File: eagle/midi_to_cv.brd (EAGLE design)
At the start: 100 x 80 mm, 75 parts, among them IC1 TL082P, IC2 TL084P, IC4 TL082P, IC6 TL082P, IC7 TL082P, U1 ATMEGA328P_PDIP, U2 MCP4822-E/P, U3 MCP4822-E/P, U4 MCP4822-E/P, U5 MCP4822-E/P

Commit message: nearly routable
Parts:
- moved R28 6.35 mm to (74.9, 43.2), turned to 270 degrees
- moved R15 5.39 mm to (12.7, 59.7), turned to 0 degrees
- moved R24 5.24 mm to (11.4, 64.8)
- moved R5 4.58 mm to (72.4, 59.7)
- moved R20 3.81 mm to (88.9, 11.4)
- moved R3 3.59 mm to (15.2, 34.3), turned to 180 degrees
- moved PAD23 2.54 mm to (21.6, 73.7)
- moved U3 2.54 mm to (20.3, 55.9)
- moved R21 2.54 mm to (83.8, 11.4)
- moved PAD6 1.80 mm to (53.3, 71.1)
- moved R29 1.80 mm to (80.0, 41.9), turned to 90 degrees
- moved IC1 1.80 mm to (53.3, 62.2)
- moved R10 1.27 mm to (41.9, 72.4)
- moved R11 1.27 mm to (58.4, 74.9)
- moved R4 1.27 mm to (50.8, 50.8)
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
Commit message: hand routing
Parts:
- moved PAD2 15.3 mm to (14.0, 15.2)
- moved PAD20 10.8 mm to (31.2, 32.3)
- moved D1 8.52 mm to (15.2, 24.1), turned to 270 degrees
- moved PAD5 5.06 mm to (90.4, 53.6)
- moved PAD12 4.58 mm to (11.4, 38.1)
- moved R3 4.02 mm to (14.0, 38.1), turned to 90 degrees
- moved R2 3.81 mm to (11.4, 25.4)
- moved R12 3.07 mm to (82.5, 53.6)
- moved PAD21 3.07 mm to (35.8, 24.1)
- moved OK1 2.84 mm to (24.1, 22.9), turned to 270 degrees
- moved PAD22 2.84 mm to (35.8, 28.7)
- moved R13 2.59 mm to (84.3, 50.8)
- moved IC2 2.54 mm to (58.4, 14.0)
- moved R1 2.54 mm to (7.62, 25.4), turned to 90 degrees
- moved PAD14 1.80 mm to (20.3, 11.4)
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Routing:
- net GND: track 0.00 -> 267.4 mm
- net +12V: track 0.00 -> 263.1 mm
- net +5V: track 0.00 -> 124.4 mm
- net -12V: track 0.00 -> 120.8 mm
- net N$41: track 0.00 -> 33.8 mm
- net N$30: track 0.00 -> 31.7 mm
- net N$59: track 0.00 -> 24.6 mm
- net N$1: track 0.00 -> 23.0 mm
- net N$22: track 0.00 -> 20.9 mm
- net N$36: track 0.00 -> 20.7 mm
- net N$35: track 0.00 -> 18.3 mm
- net N$50: track 0.00 -> 18.3 mm
- net N$18: track 0.00 -> 17.9 mm
- net N$39: track 0.00 -> 17.6 mm
- net N$27: track 0.00 -> 17.1 mm
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
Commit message: manually routed and vias adjusted
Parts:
- moved PAD18 4.57 mm to (49.5, 13.5)
- moved PAD16 4.07 mm to (67.1, 16.3)
- moved PAD11 3.66 mm to (55.1, 51.3)
- moved R4 2.59 mm to (48.3, 51.3)
- moved PAD8 2.29 mm to (67.3, 21.8)
- moved R16 2.05 mm to (71.6, 11.2), turned to 270 degrees
- moved PAD7 1.61 mm to (67.8, 6.10)
- moved PAD10 1.27 mm to (49.5, 6.35)
- moved R3 1.05 mm to (14.2, 39.1)
- moved R28 0.92 mm to (74.4, 42.4)
- moved PAD4 0.51 mm to (47.0, 74.4)
- moved R18 0.51 mm to (36.8, 10.7)
- moved R19 0.51 mm to (44.5, 10.7)
- moved R22 0.51 mm to (33.0, 10.7)
- moved R23 0.51 mm to (40.6, 10.7)
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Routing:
- net -12V: track 120.8 -> 233.8 mm, vias 0 -> 6
- net +5V: track 124.4 -> 218.0 mm, vias 0 -> 4
- net GND: track 267.4 -> 324.0 mm
- net N$42: track 5.08 -> 30.2 mm
- net N$24: track 0.00 -> 24.8 mm, vias 0 -> 2
- net N$37: track 0.00 -> 20.9 mm
- net N$39: track 17.6 -> 38.2 mm
- net +12V: track 263.1 -> 278.8 mm, vias 0 -> 2
- net N$61: track 0.00 -> 11.8 mm
- net N$40: track 11.7 -> 23.0 mm
- net N$38: track 0.00 -> 10.2 mm
- net N$35: track 18.3 -> 9.44 mm
- net N$56: track 0.00 -> 7.32 mm
- net N$34: track 0.00 -> 5.92 mm
- net N$44: track 0.00 -> 5.61 mm
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
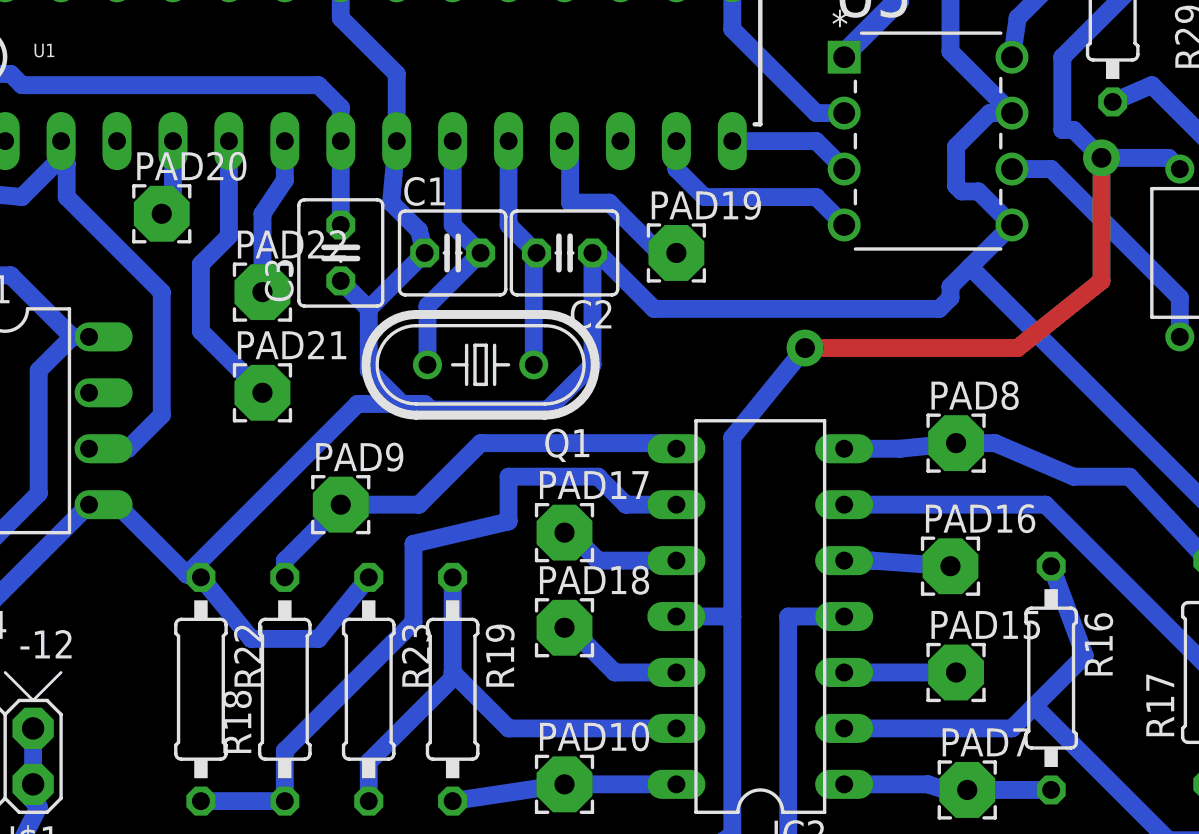
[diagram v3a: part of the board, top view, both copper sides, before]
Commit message: will route gates to op amps instead of jumper pads
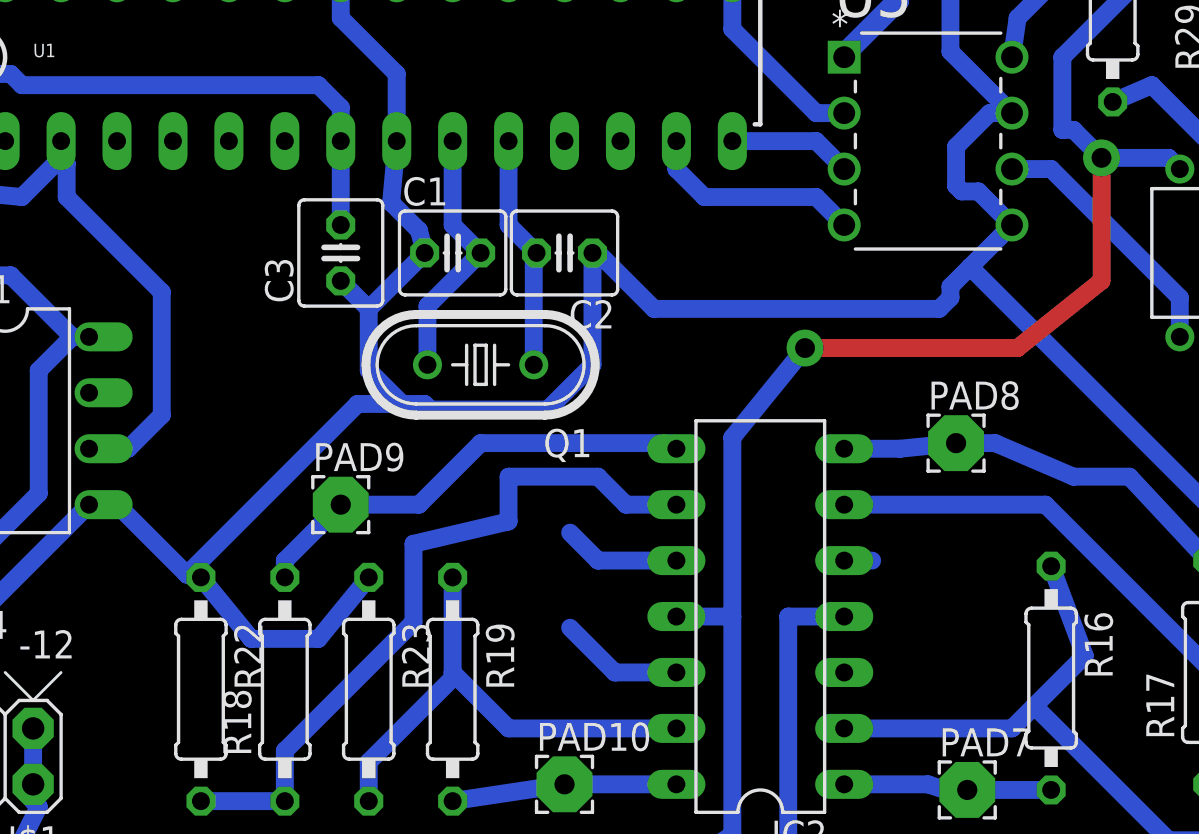
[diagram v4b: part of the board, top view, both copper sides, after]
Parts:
- removed PAD15, PAD16, PAD17, PAD18, PAD19, PAD20, PAD21, PAD22: gate, wirepad:2,54/0,9
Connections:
- removed net N$31: PAD19.1, U1.11
- removed net N$32: PAD20.1, U1.4
- removed net N$33: PAD21.1, U1.5
- removed net N$43: PAD22.1, U1.6
- net N$34: now also U1.11; no longer PAD18.1
- net N$44: now also U1.6; no longer PAD17.1
- net N$45: now also U1.5; no longer PAD16.1
- net N$46: now also U1.4; no longer PAD15.1
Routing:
- net N$33: track 13.1 -> 0.00 mm
- net N$31: track 8.67 -> 0.00 mm
- net N$43: track 7.17 -> 0.00 mm
- net N$46: track 5.08 -> 0.00 mm
- net N$45: track 4.84 -> 1.27 mm
- net N$32: track 3.51 -> 0.00 mm
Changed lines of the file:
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@@
 <element name="PAD13" library="wirepad" package="2,54/0,9" value="reset " x="69.85" y="73.66"/>
 <element name="PAD14" library="wirepad" package="2,54/0,9" value="gate LED" x="20.32" y="11.43"/>
-<element name="PAD15" library="wirepad" package="2,54/0,9" value="gate" x="67.31" y="11.43"/>
-<element name="PAD16" library="wirepad" package="2,54/0,9" value="gate" x="67.056" y="16.256"/>
-<element name="PAD17" library="wirepad" package="2,54/0,9" value="gate" x="49.53" y="17.78"/>
-<element name="PAD18" library="wirepad" package="2,54/0,9" value="gate" x="49.53" y="13.462"/>
-<element name="PAD19" library="wirepad" package="2,54/0,9" value="gate" x="54.61" y="30.48"/>
-<element name="PAD20" library="wirepad" package="2,54/0,9" value="gate" x="31.242" y="32.258"/>
-<element name="PAD21" library="wirepad" package="2,54/0,9" value="gate" x="35.814" y="24.13"/>
-<element name="PAD22" library="wirepad" package="2,54/0,9" value="gate" x="35.814" y="28.702"/>
 <element name="R8" library="rcl" package="0207/10" value="3.3k" x="39.624" y="60.198"/>
 <element name="R9" library="pot" package="B64W" value="10k" x="43.18" y="66.04" rot="R270"/>
@@
 <wire x1="54.61" y1="50.8" x2="55.118" y2="51.308" width="0.8128" layer="16"/>
 </signal>
-<signal name="N$32">
-<contactref element="U1" pad="4"/>
-<contactref element="PAD20" pad="1"/>
-<wire x1="31.75" y1="35.56" x2="31.75" y2="32.766" width="0.8128" layer="16"/>
-<wire x1="31.75" y1="32.766" x2="31.242" y2="32.258" width="0.8128" layer="16"/>
-</signal>
-<signal name="N$33">
-<contactref element="U1" pad="5"/>
-<contactref element="PAD21" pad="1"/>
-<wire x1="34.29" y1="35.56" x2="34.29" y2="31.242" width="0.8128" layer="16"/>
-<wire x1="34.29" y1="31.242" x2="33.02" y2="29.972" width="0.8128" layer="16"/>
-<wire x1="33.02" y1="29.972" x2="33.02" y2="26.924" width="0.8128" layer="16"/>
-<wire x1="33.02" y1="26.924" x2="35.814" y2="24.13" width="0.8128" layer="16"/>
-</signal>
 <signal name="N$34">
 <contactref element="IC2" pad="12"/>
-<contactref element="PAD18" pad="1"/>
-<wire x1="49.53" y1="13.462" x2="49.784" y2="13.462" width="0.8128" layer="16"/>
 <wire x1="49.784" y1="13.462" x2="51.816" y2="11.43" width="0.8128" layer="16"/>
 <wire x1="51.816" y1="11.43" x2="54.61" y2="11.43" width="0.8128" layer="16"/>
+<contactref element="U1" pad="11"/>
+<wire x1="49.784" y1="13.462" x2="49.53" y2="35.56" width="0" layer="19" extent="16-16"/>
 </signal>
 <signal name="N$35">
@@
 <wire x1="78.74" y1="6.858" x2="79.248" y2="6.35" width="0.8128" layer="16"/>
 </signal>
-<signal name="N$43">
-<contactref element="U1" pad="6"/>
-<contactref element="PAD22" pad="1"/>
-<wire x1="35.814" y1="28.702" x2="35.814" y2="32.258" width="0.8128" layer="16"/>
-<wire x1="35.814" y1="32.258" x2="36.83" y2="33.782" width="0.8128" layer="16"/>
-<wire x1="36.83" y1="33.782" x2="36.83" y2="35.56" width="0.8128" layer="16"/>
-</signal>
 <signal name="N$44">
 <contactref element="IC2" pad="10"/>
-<contactref element="PAD17" pad="1"/>
-<wire x1="49.53" y1="17.78" x2="49.784" y2="17.78" width="0.8128" layer="16"/>
 <wire x1="49.784" y1="17.78" x2="51.054" y2="16.51" width="0.8128" layer="16"/>
 <wire x1="51.054" y1="16.51" x2="54.61" y2="16.51" width="0.8128" layer="16"/>
+<contactref element="U1" pad="6"/>
+<wire x1="49.784" y1="17.78" x2="36.83" y2="35.56" width="0" layer="19" extent="16-16"/>
 </signal>
 <signal name="N$45">
 <contactref element="IC2" pad="5"/>
-<contactref element="PAD16" pad="1"/>
 <wire x1="62.23" y1="16.51" x2="63.5" y2="16.51" width="0.8128" layer="16"/>
-<wire x1="63.5" y1="16.51" x2="67.056" y2="16.256" width="0.8128" layer="16"/>
+<contactref element="U1" pad="5"/>
+<wire x1="34.29" y1="35.56" x2="62.23" y2="16.51" width="0" layer="19" extent="1-1"/>
 </signal>
 <signal name="N$46">
-<contactref element="PAD15" pad="1"/>
 <contactref element="IC2" pad="3"/>
-<wire x1="62.23" y1="11.43" x2="67.31" y2="11.43" width="0.8128" layer="16"/>
+<contactref element="U1" pad="4"/>
+<wire x1="31.75" y1="35.56" x2="62.23" y2="11.43" width="0" layer="19" extent="1-1"/>
 </signal>
 <signal name="N$51">
@@
 <wire x1="77.47" y1="28.448" x2="77.47" y2="26.67" width="0.8128" layer="16"/>
 </signal>
-<signal name="N$31">
-<contactref element="U1" pad="11"/>
-<contactref element="PAD19" pad="1"/>
-<wire x1="54.61" y1="30.48" x2="53.848" y2="30.48" width="0.8128" layer="16"/>
-<wire x1="53.848" y1="30.48" x2="51.562" y2="32.766" width="0.8128" layer="16"/>
-<wire x1="51.562" y1="32.766" x2="49.784" y2="32.766" width="0.8128" layer="16"/>
-<wire x1="49.784" y1="32.766" x2="49.784" y2="35.306" width="0.8128" layer="16"/>
-<wire x1="49.784" y1="35.306" x2="49.53" y2="35.56" width="0.8128" layer="16"/>
-</signal>
 <signal name="N$62">

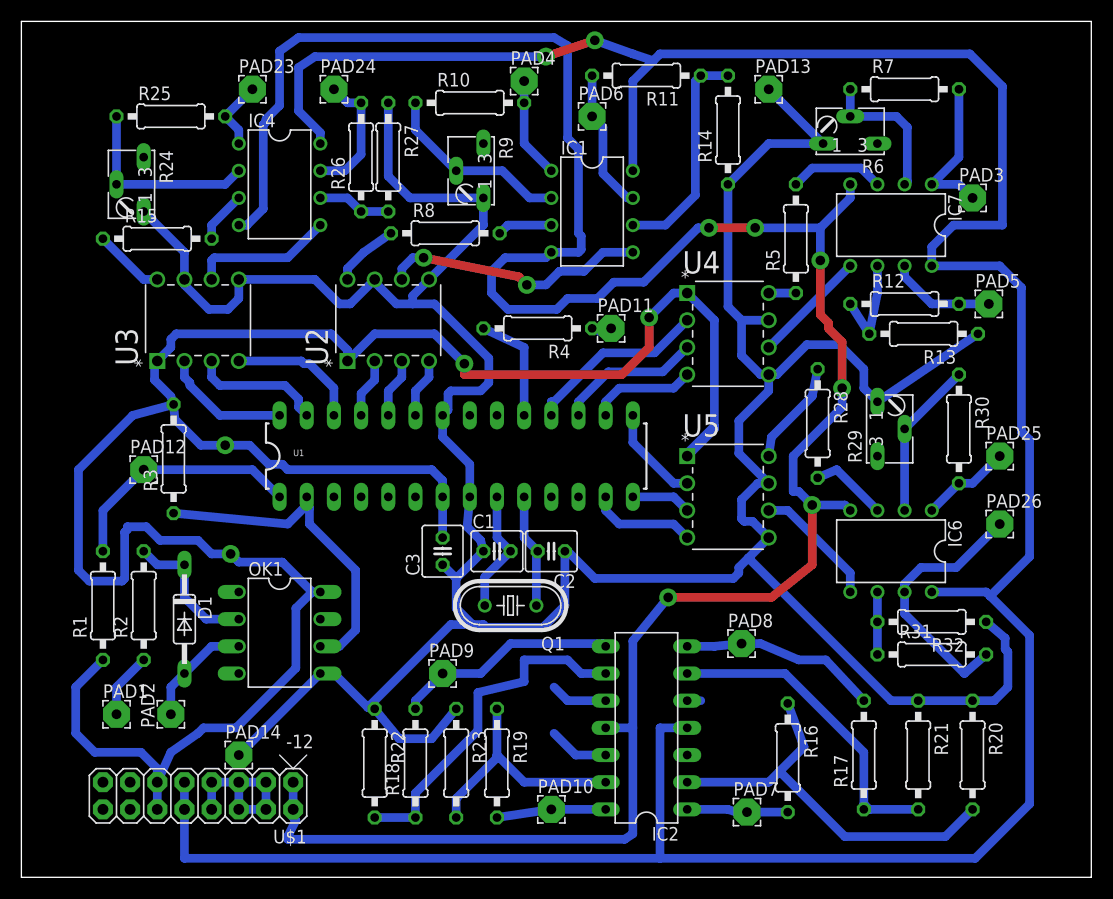
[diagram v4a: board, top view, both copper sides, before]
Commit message: routed with vias to gates
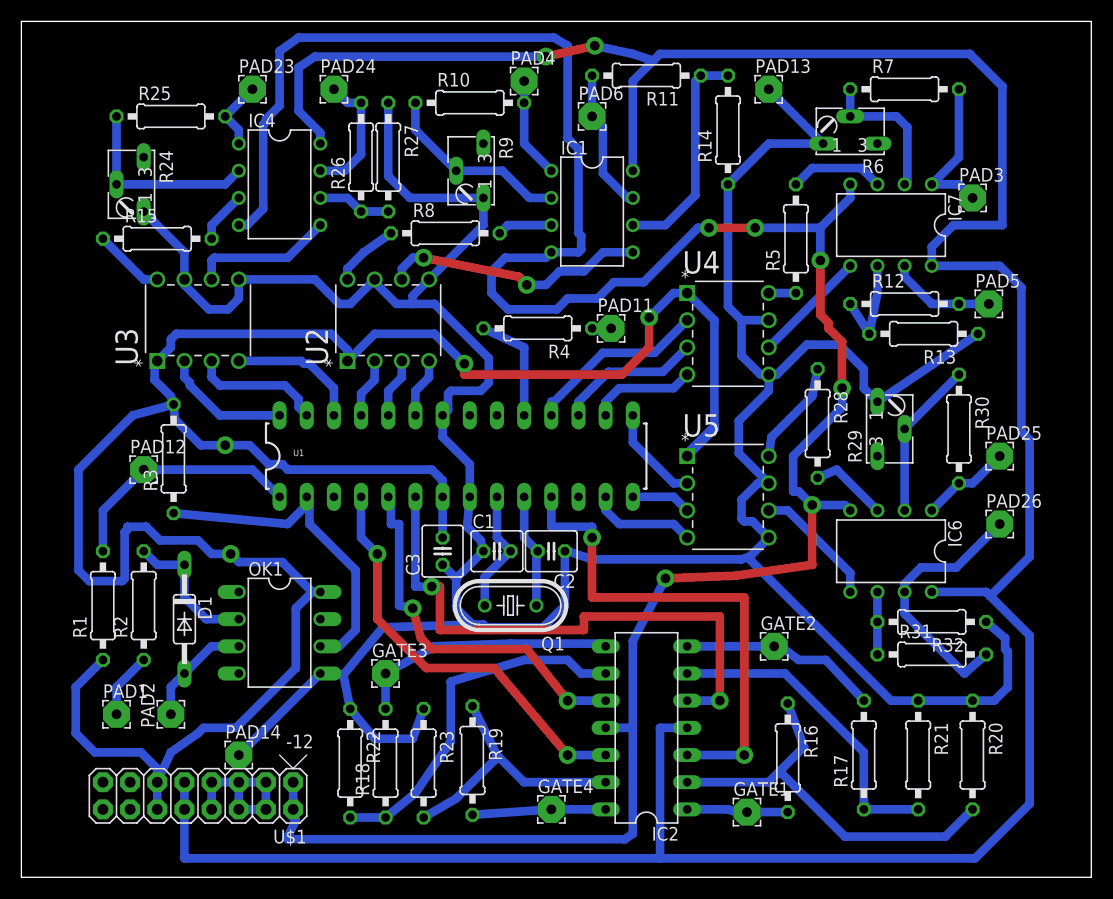
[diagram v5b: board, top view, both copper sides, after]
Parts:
- removed PAD8, PAD9: gate output, wirepad:2,54/0,9
- added GATE2, GATE3: gate output, wirepad:2,54/0,9
- moved R23 3.05 mm to (37.6, 10.7)
- moved R18 2.79 mm to (34.0, 10.7)
- moved R19 2.30 mm to (42.2, 10.9)
- moved R22 2.29 mm to (30.7, 10.7)
- renumbered PAD10 to GATE4, PAD7 to GATE1
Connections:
- removed net N$34: IC2.12, U1.11
- removed net N$44: IC2.10, U1.6
- new net N$32: IC2.3, U1.11
- new net N$33: IC2.5, U1.6
- net N$36: now also GATE2.1; no longer PAD8.1
- net N$37: now also GATE3.1; no longer PAD9.1
- net N$45: now also IC2.10; no longer IC2.5
- net N$46: now also IC2.12; no longer IC2.3
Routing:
- net N$33: track 0.00 -> 53.1 mm, vias 0 -> 2
- net N$32: track 0.00 -> 47.5 mm, vias 0 -> 2
- net N$46: track 0.00 -> 39.1 mm, vias 0 -> 2
- net N$45: track 1.27 -> 35.4 mm, vias 0 -> 2
- net N$34: track 5.67 -> 0.00 mm
- net N$44: track 5.35 -> 0.00 mm
- net N$37: track 20.9 -> 24.6 mm
- net N$40: track 23.0 -> 25.5 mm
- net N$38: track 10.2 -> 12.5 mm
- net GND: track 324.0 -> 322.2 mm
- net N$41: track 32.5 -> 33.6 mm
- net -12V: track 233.8 -> 234.4 mm
